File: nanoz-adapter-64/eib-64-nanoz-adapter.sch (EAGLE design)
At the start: 4 parts, among them J1 DF40-REC, J4 SCREW2

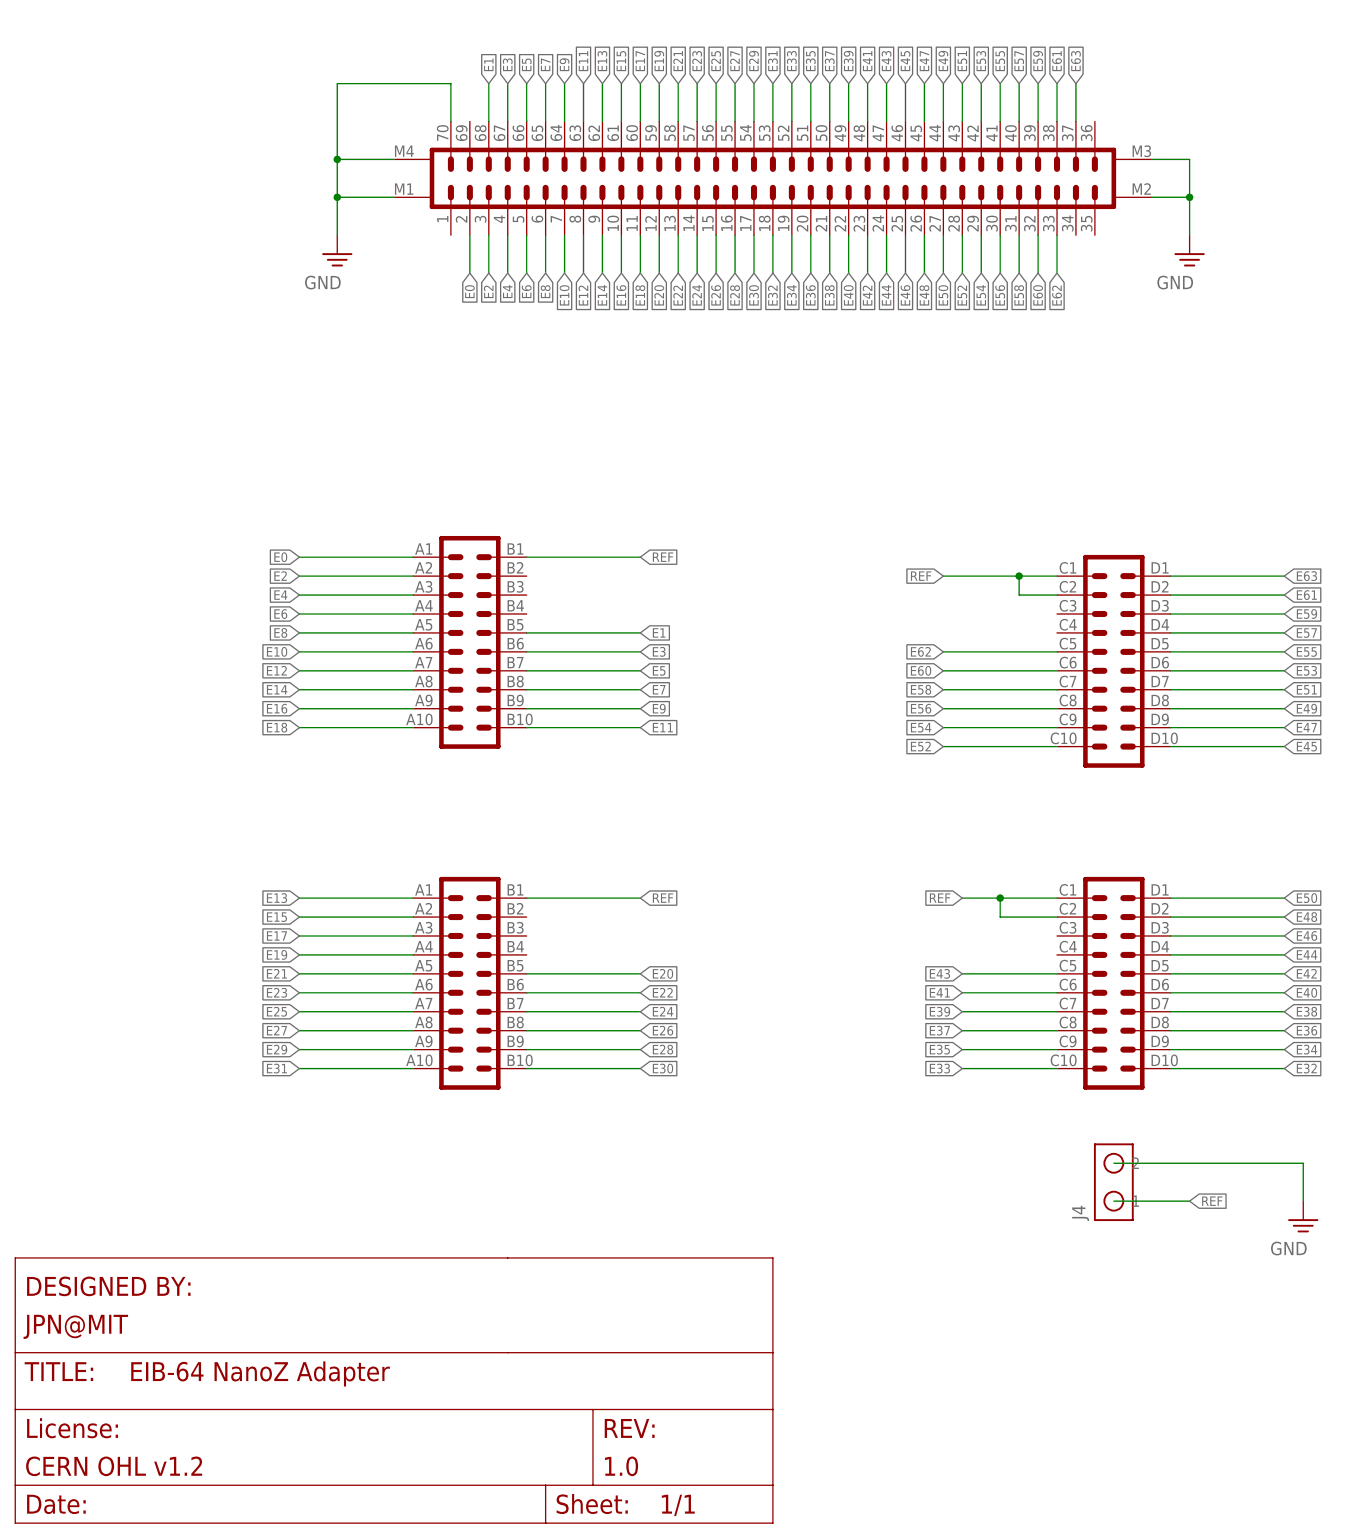
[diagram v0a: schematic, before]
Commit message: Switched the side of headstage connector on nanoz-adapter-64
- The drive would have barely extended below the bottom edge of the
nanoz in the previous orientation
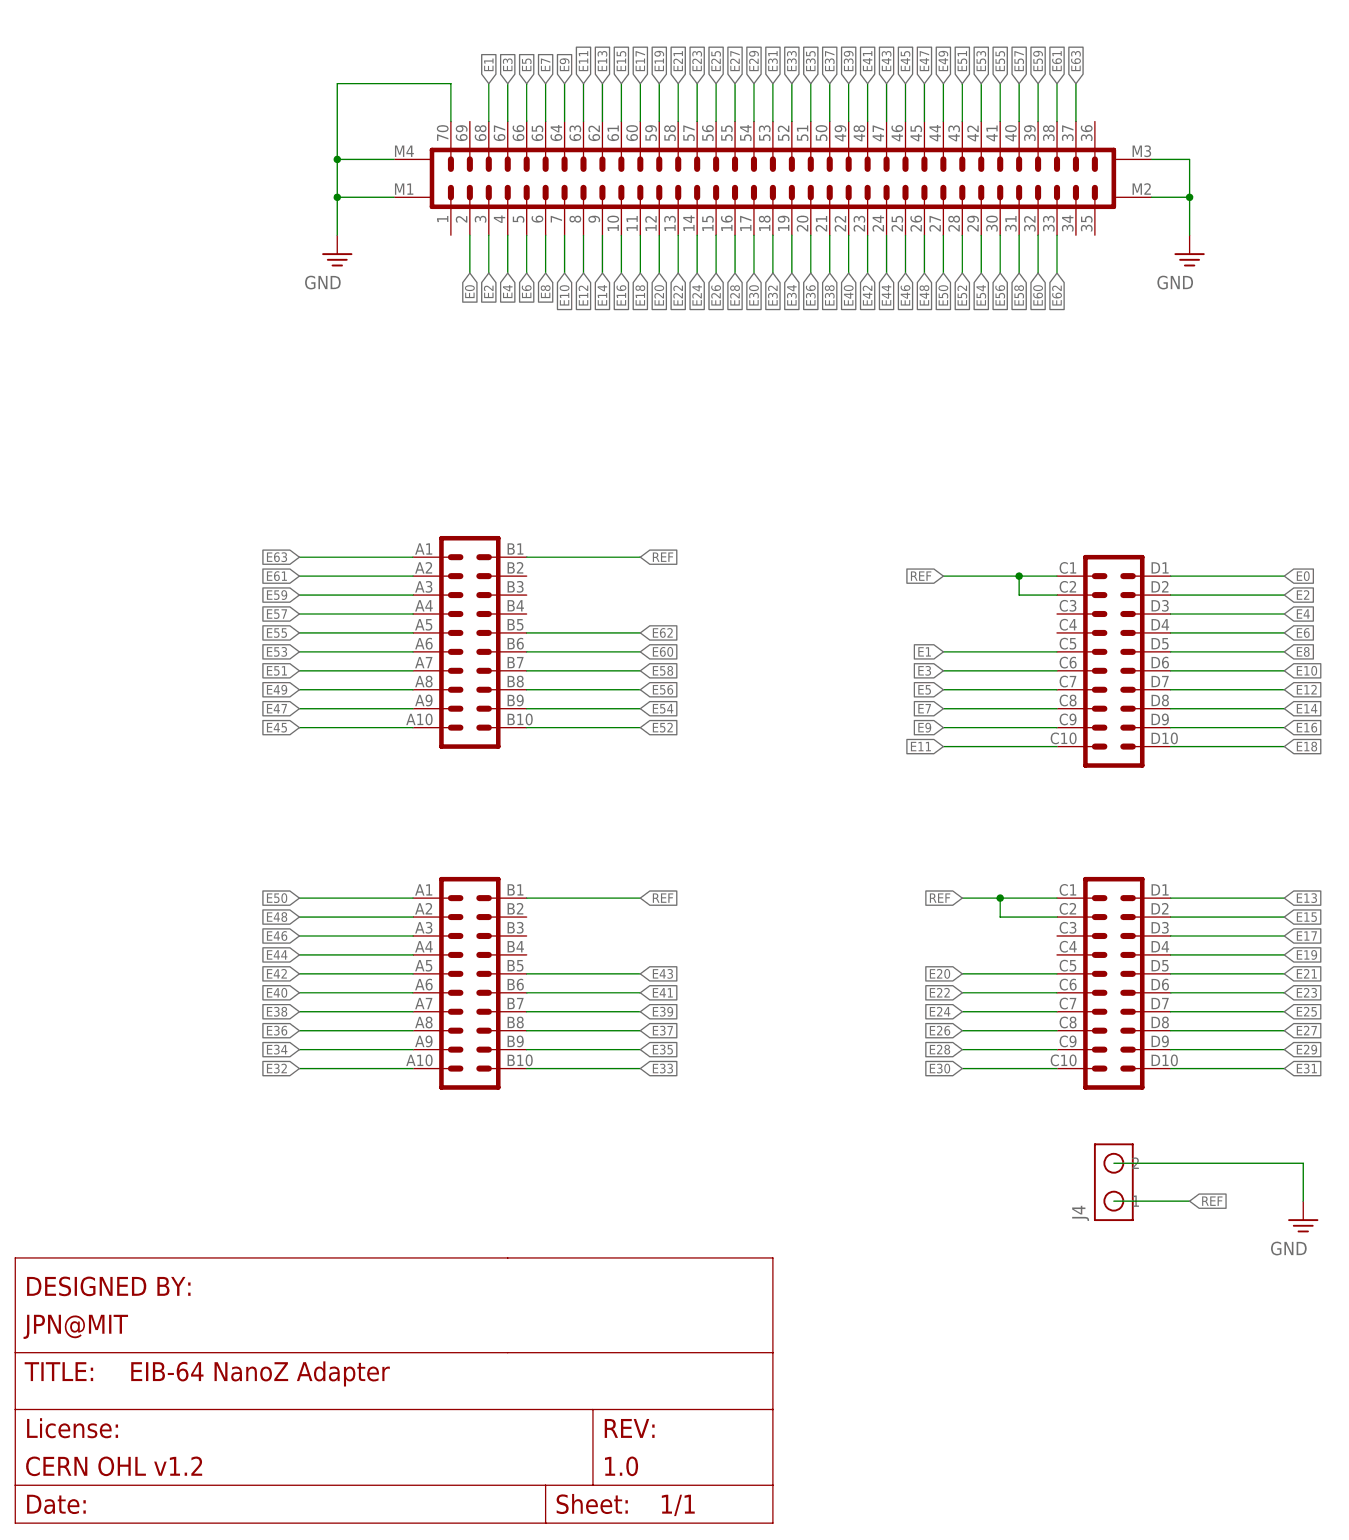
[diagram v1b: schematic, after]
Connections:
- net E0: now also J2G$2.20; no longer J2G$1.1
- net E1: now also J2G$2.5; no longer J2G$1.16
- net E10: now also J2G$2.15; no longer J2G$1.6
- net E11: now also J2G$2.10; no longer J2G$1.11
- net E12: now also J2G$2.14; no longer J2G$1.7
- net E13: now also J3G$2.20; no longer J3G$1.1
- net E14: now also J2G$2.13; no longer J2G$1.8
- net E15: now also J3G$2.19; no longer J3G$1.2
- net E16: now also J2G$2.12; no longer J2G$1.9
- net E17: now also J3G$2.18; no longer J3G$1.3
- net E18: now also J2G$2.11; no longer J2G$1.10
- net E19: now also J3G$2.17; no longer J3G$1.4
- net E2: now also J2G$2.19; no longer J2G$1.2
- net E20: now also J3G$2.5; no longer J3G$1.16
- net E21: now also J3G$2.16; no longer J3G$1.5
- net E22: now also J3G$2.6; no longer J3G$1.15
- net E23: now also J3G$2.15; no longer J3G$1.6
- net E24: now also J3G$2.7; no longer J3G$1.14
- net E25: now also J3G$2.14; no longer J3G$1.7
- net E26: now also J3G$2.8; no longer J3G$1.13
- net E27: now also J3G$2.13; no longer J3G$1.8
- net E28: now also J3G$2.9; no longer J3G$1.12
- net E29: now also J3G$2.12; no longer J3G$1.9
- net E3: now also J2G$2.6; no longer J2G$1.15
- net E30: now also J3G$2.10; no longer J3G$1.11
- net E31: now also J3G$2.11; no longer J3G$1.10
- net E32: now also J3G$1.10; no longer J3G$2.11
- net E33: now also J3G$1.11; no longer J3G$2.10
- net E34: now also J3G$1.9; no longer J3G$2.12
- net E35: now also J3G$1.12; no longer J3G$2.9
- net E36: now also J3G$1.8; no longer J3G$2.13
- net E37: now also J3G$1.13; no longer J3G$2.8
- net E38: now also J3G$1.7; no longer J3G$2.14
- net E39: now also J3G$1.14; no longer J3G$2.7
- net E4: now also J2G$2.18; no longer J2G$1.3
- net E40: now also J3G$1.6; no longer J3G$2.15
- net E41: now also J3G$1.15; no longer J3G$2.6
- net E42: now also J3G$1.5; no longer J3G$2.16
- net E43: now also J3G$1.16; no longer J3G$2.5
- net E44: now also J3G$1.4; no longer J3G$2.17
- net E45: now also J2G$1.10; no longer J2G$2.11
- net E46: now also J3G$1.3; no longer J3G$2.18
- net E47: now also J2G$1.9; no longer J2G$2.12
- net E48: now also J3G$1.2; no longer J3G$2.19
- net E49: now also J2G$1.8; no longer J2G$2.13
- net E5: now also J2G$2.7; no longer J2G$1.14
- net E50: now also J3G$1.1; no longer J3G$2.20
- net E51: now also J2G$1.7; no longer J2G$2.14
- net E52: now also J2G$1.11; no longer J2G$2.10
- net E53: now also J2G$1.6; no longer J2G$2.15
- net E54: now also J2G$1.12; no longer J2G$2.9
- net E55: now also J2G$1.5; no longer J2G$2.16
- net E56: now also J2G$1.13; no longer J2G$2.8
- net E57: now also J2G$1.4; no longer J2G$2.17
- net E58: now also J2G$1.14; no longer J2G$2.7
- net E59: now also J2G$1.3; no longer J2G$2.18
- net E6: now also J2G$2.17; no longer J2G$1.4
- net E60: now also J2G$1.15; no longer J2G$2.6
- net E61: now also J2G$1.2; no longer J2G$2.19
- net E62: now also J2G$1.16; no longer J2G$2.5
- net E63: now also J2G$1.1; no longer J2G$2.20
- net E7: now also J2G$2.8; no longer J2G$1.13
- net E8: now also J2G$2.16; no longer J2G$1.5
- net E9: now also J2G$2.9; no longer J2G$1.12

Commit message: headstage-64 rev. 1.4 along with all dependencies
- This is headstage-64 revision 1.4. Because it involves a change in the
bottom analog connector, a lot of other boards had to be changed to
match the new pinout. That is why there are so many files in this
commit. Changes in revision 1.4 and affects on other boards are as
follows:

1. The coaxial adapter board has been improved to allow a regulator to
sit on the daughter board. To do this, the filtered vcoax had to brought
back to the daughter board and then out again after regulation. Of
course this regulation can be bypassed simply by connecting these
contacts

2. Vcoax decoupling has been greatly improved to lower impedance of
power input. There is now 70 uF of decoupling capacitance on the
post-regulated vcoax.

3. The JTAG interface was changed to allow it to be enabled and disabled
by the programmer. This means that these pins are nominally used for
extra IO. The programmer now contains a jumper that allows it operate in
this new mode (closed) or legacy mode (open) for headstage-64 rev 1.3.

4. All of the serializers GPIO lines are now all routed to the FPGA.

5. The opto and estim circuits no longer share SPI lines so they can be
operated independently.

6. The analog routing to the intan chip has been changed such that the
electrode lines are shielded from vcoax, which was polluting the anlog
signals, by a ground pin. This means that eibs etc. need to respect this
new pinout. This is why eib-64, eib-64-large, nanoz-adapter,
omnetics-adapter-64, and test-board-64 have been changed.

7. The serializer on headstage-64 has been upgraded to DS90UB933-Q1
which has reduced back channel latencies, increased forward channel
bandwidth, and improved performance with
imperfect cabling.

8. There is a solder jumper on the bottom of headstage-64 to allow the
addition of an external resistor to AUXIN3 on the intan to allow it to
operate at lower bandwidths. This comes at the cost of not being able to
measure istim unless t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
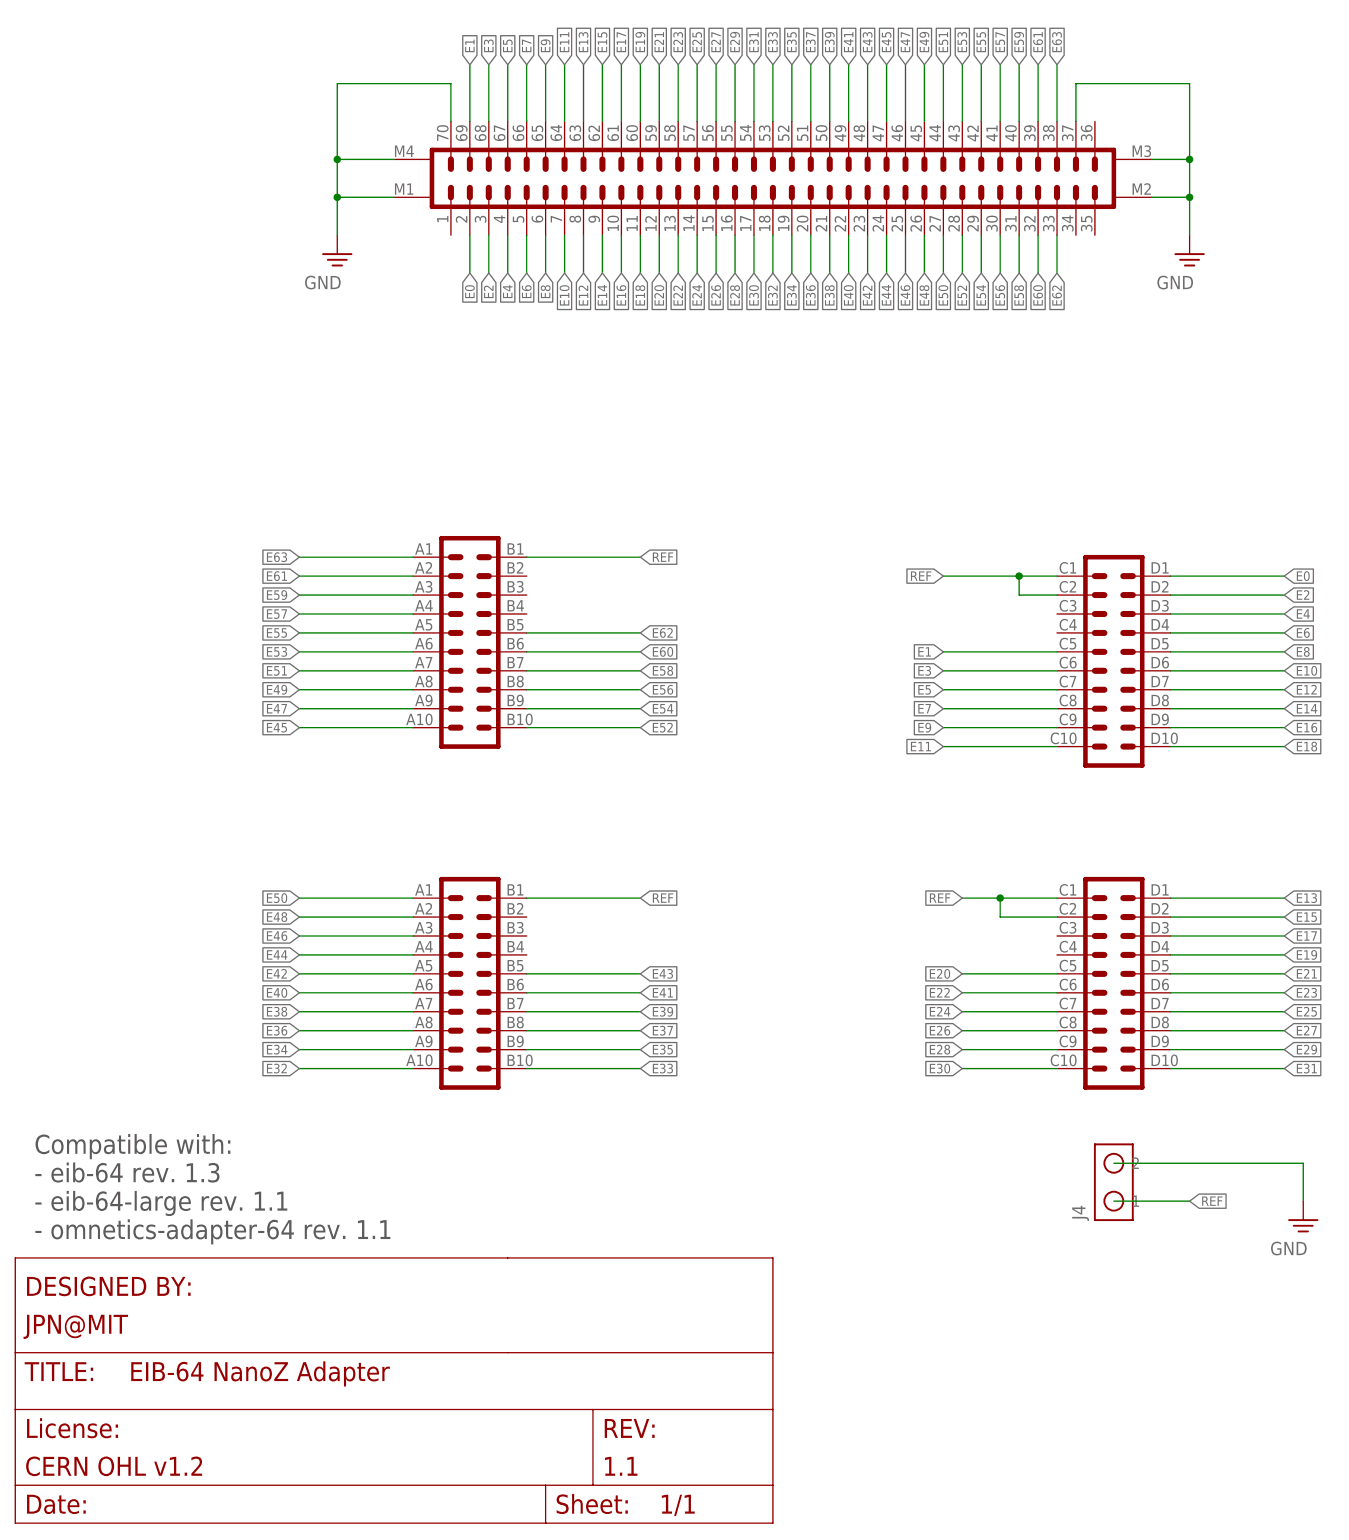
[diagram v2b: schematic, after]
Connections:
- net E1: now also J1.69; no longer J1.68
- net E11: now also J1.64; no longer J1.63
- net E13: now also J1.63; no longer J1.62
- net E15: now also J1.62; no longer J1.61
- net E17: now also J1.61; no longer J1.60
- net E19: now also J1.60; no longer J1.59
- net E21: now also J1.59; no longer J1.58
- net E23: now also J1.58; no longer J1.57
- net E25: now also J1.57; no longer J1.56
- net E27: now also J1.56; no longer J1.55
- net E29: now also J1.55; no longer J1.54
- net E3: now also J1.68; no longer J1.67
- net E31: now also J1.54; no longer J1.53
- net E33: now also J1.53; no longer J1.52
- net E35: now also J1.52; no longer J1.51
- net E37: now also J1.51; no longer J1.50
- net E39: now also J1.50; no longer J1.49
- net E41: now also J1.49; no longer J1.48
- net E43: now also J1.48; no longer J1.47
- net E45: now also J1.47; no longer J1.46
- net E47: now also J1.46; no longer J1.45
- net E49: now also J1.45; no longer J1.44
- net E5: now also J1.67; no longer J1.66
- net E51: now also J1.44; no longer J1.43
- net E53: now also J1.43; no longer J1.42
- net E55: now also J1.42; no longer J1.41
- net E57: now also J1.41; no longer J1.40
- net E59: now also J1.40; no longer J1.39
- net E61: now also J1.39; no longer J1.38
- net E63: now also J1.38; no longer J1.37
- net E7: now also J1.66; no longer J1.65
- net E9: now also J1.65; no longer J1.64
- net GND: now also J1.37
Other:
- note added: "Compatible with: - eib-64 rev. 1.3 - eib-64-large rev. 1.1 - omnetics-adapter-64 rev. 1.1"
